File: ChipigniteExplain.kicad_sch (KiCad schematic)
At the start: 73 parts, among them J1 Conn_01x02, J2 Conn_01x02, J3 Conn_01x03, J4 USB_C, J5 613012243121, J6 613012243121, J7 Conn_02x03_Odd_Even, Q1 DMN2005K, SW1 434121025816, SW2 434121025816, SW6 193-8MSR, U1 TLV1117LV33, U2 TPD1E05U06QDPYRQ1, U3 157112V12700

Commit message: title + attrib
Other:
- note added: "ChipIgnite/Efabless Explain FPGA ASIC Teaching Board"
- note removed: "Efabless Explain FPGA ASIC Teaching Board"
- company: Psychogenic Technologies  -> Psychogenic Technologies for efabless
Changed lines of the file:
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@@
 		(date "2025-02-21")
 		(rev "1.1")
-		(company "Psychogenic Technologies ")
+		(company "Psychogenic Technologies for efabless")
 		(comment 1 "(C) 2024-2025 Pat Deegan")
 	)
@@
 		)
 	)
-	(text "Efabless Explain FPGA ASIC Teaching Board"
+	(text "ChipIgnite/Efabless Explain FPGA ASIC Teaching Board"
 		(exclude_from_sim no)
-		(at 156.21 17.526 0)
+		(at 146.304 17.526 0)
 		(effects
 			(font

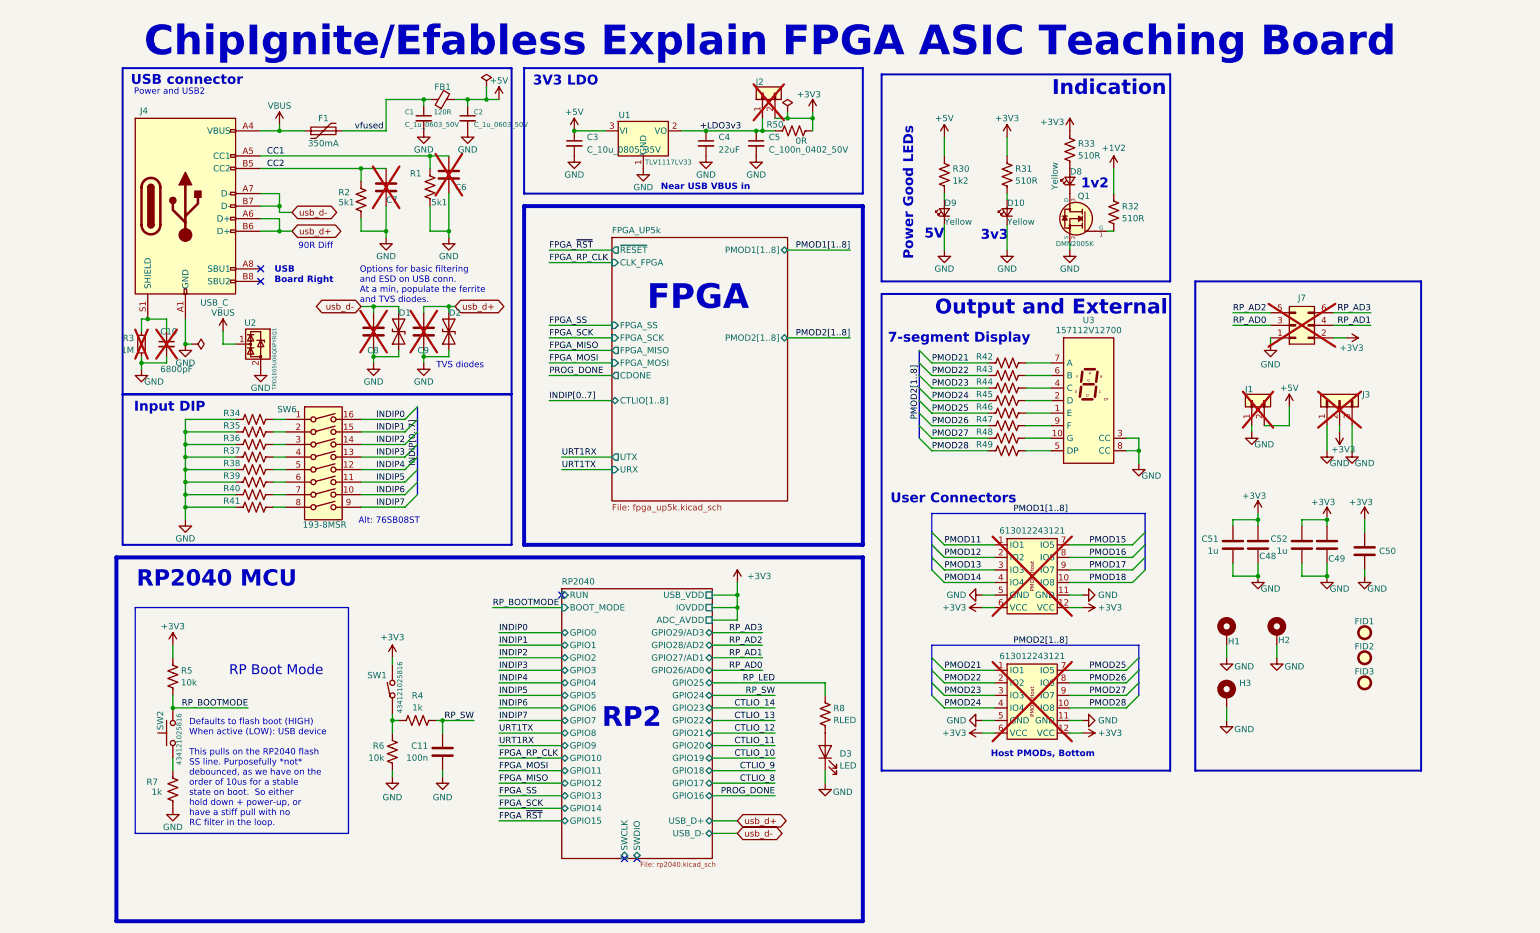
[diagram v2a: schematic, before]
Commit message: BOM MPN additions and tweaks
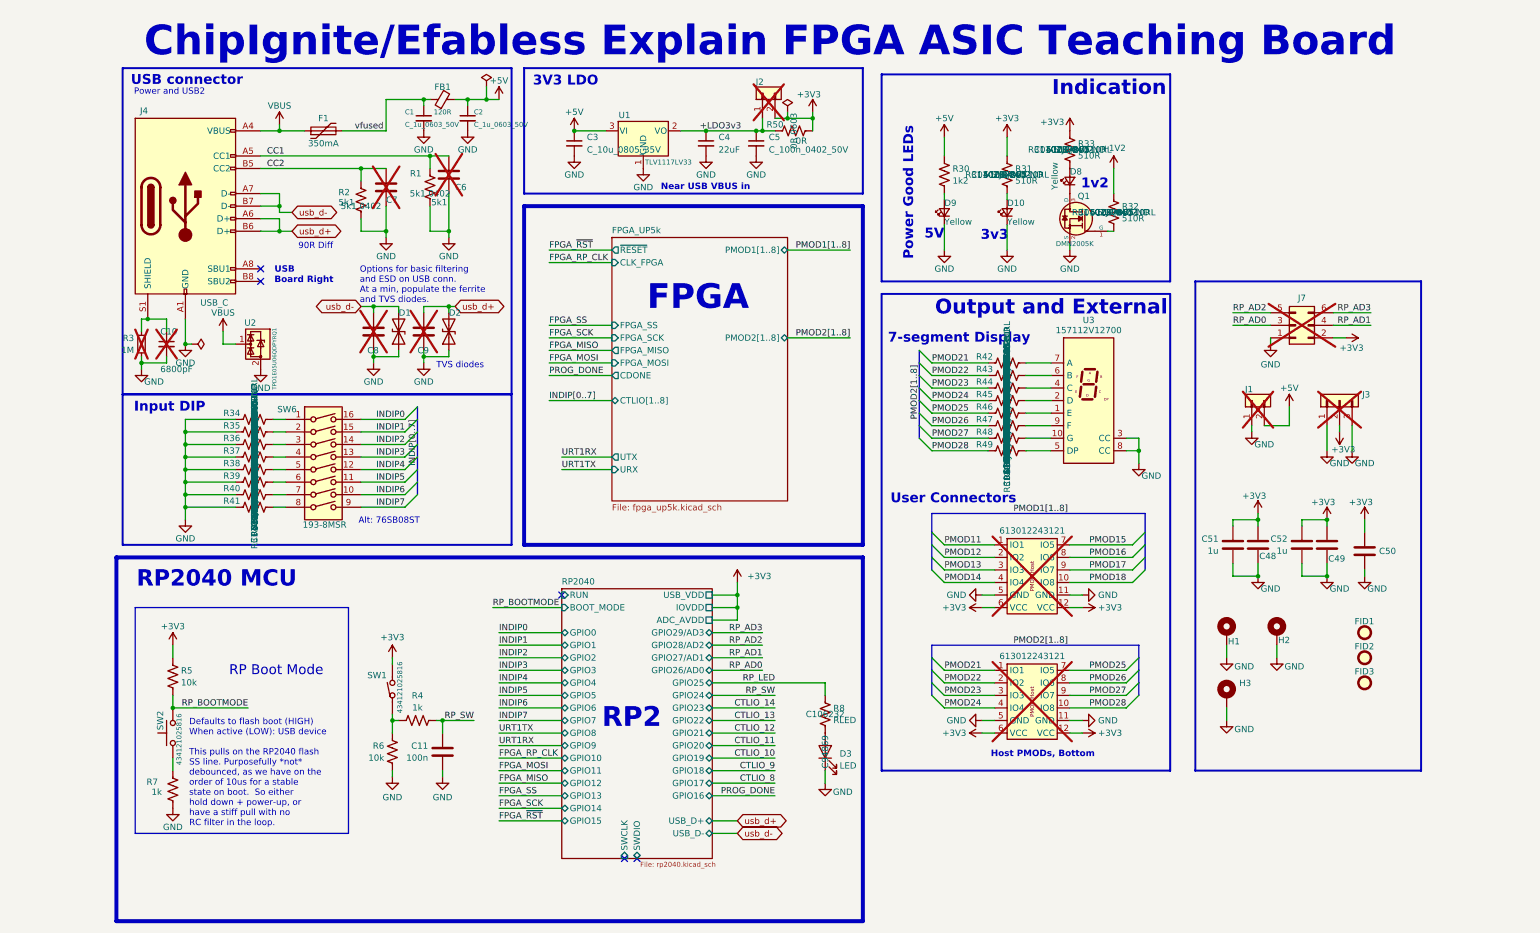
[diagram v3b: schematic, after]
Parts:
- D3: DigikeyPN (none) -> 160-1436-1-ND; LCSC (none) -> C94869; MPN (none) -> LTST-C190KRKT; MPN_ALT (none) -> EAST16084RA0
- R1, R2: Characteristics (none) -> 5k1 0402
- R31, R32, R33, R34, R35, R36, R37, R38, R39, R40, R41, R42, R43, R44, R45, R46, R47, R48, R49: Characteristics (none) -> 510R 0402; DigikeyPN (none) -> 311-510JRCT-ND; LCSC (none) -> C137860; MPN (none) -> RC0402JR-07510RL
- R4: Characteristics R 0402 1k5 1% -> 1k 0402
- R50: Characteristics (none) -> 0R 0603
- R7: Characteristics (none) -> 1k 0402
- R8: Characteristics (none) -> 100R 0402; DigikeyPN (none) -> 311-100LRCT-ND; LCSC (none) -> C106232; MPN (none) -> RC0402FR-07100RL
- SW1: Characteristics SWITCH TACTILE SPST-NO -> MOM SPST NO
